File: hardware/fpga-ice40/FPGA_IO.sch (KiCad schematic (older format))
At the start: 1 part, among them U1 iCE40HX4K-TQ144

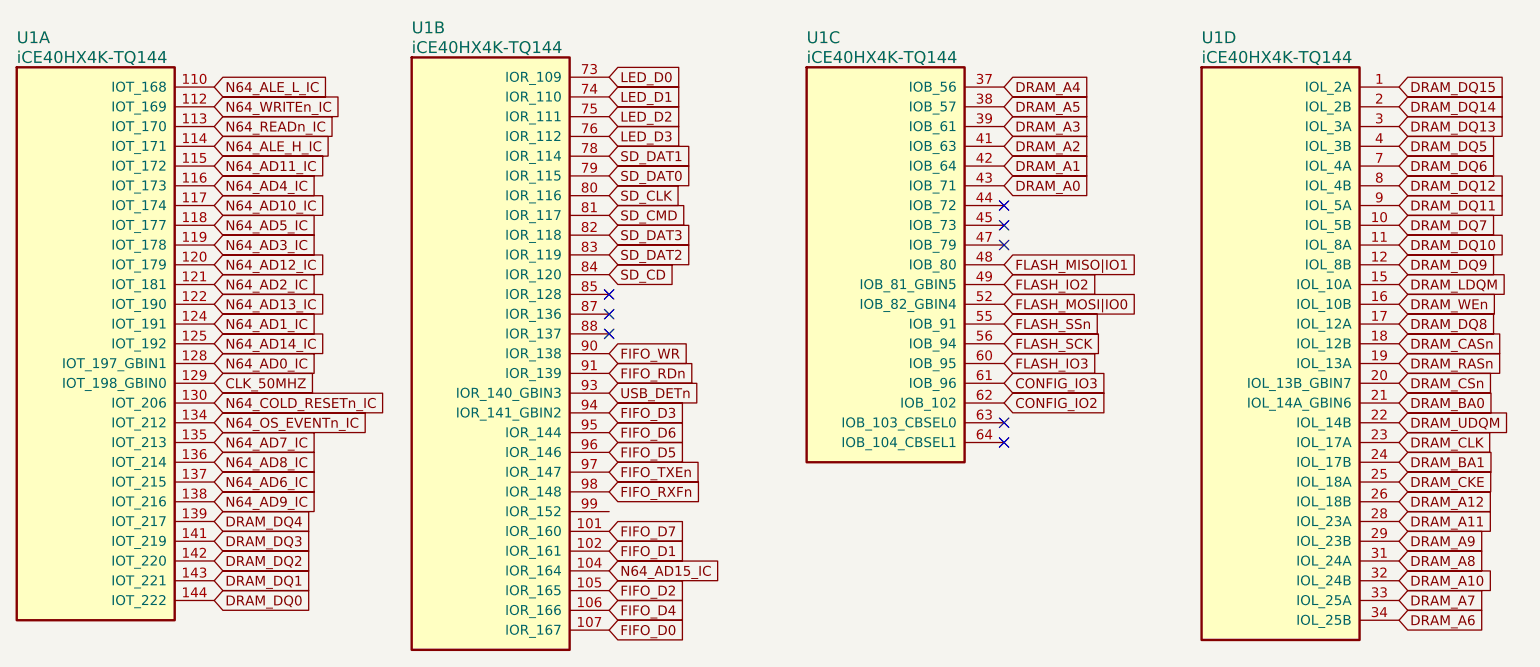
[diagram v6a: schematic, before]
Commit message: Routed N64, DRAM, FIFO, and SD card interfaces
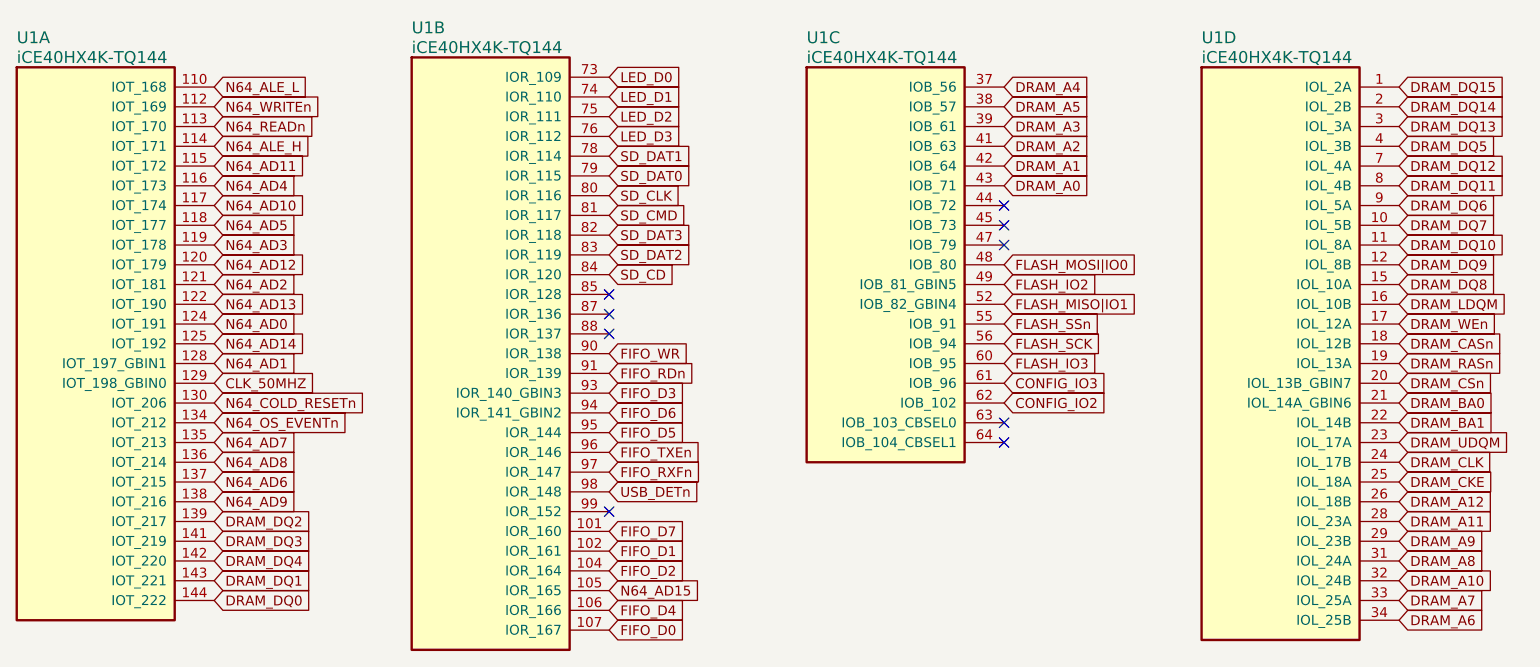
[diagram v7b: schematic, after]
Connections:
- net N64_AD15_IC is gone; now on net FIFO_D2: U1.104 (IOR_164)
- net DRAM_BA1: now also U1.22 (IOL_14B); no longer U1.24 (IOL_17B)
- net DRAM_CLK: now also U1.24 (IOL_17B); no longer U1.23 (IOL_17A)
- net DRAM_DQ11: now also U1.8 (IOL_4B); no longer U1.9 (IOL_5A)
- net DRAM_DQ12: now also U1.7 (IOL_4A); no longer U1.8 (IOL_4B)
- net DRAM_DQ2: now also U1.139 (IOT_217); no longer U1.142 (IOT_220)
- net DRAM_DQ4: now also U1.142 (IOT_220); no longer U1.139 (IOT_217)
- net DRAM_DQ6: now also U1.9 (IOL_5A); no longer U1.7 (IOL_4A)
- net DRAM_DQ8: now also U1.15 (IOL_10A); no longer U1.17 (IOL_12A)
- net DRAM_LDQM: now also U1.16 (IOL_10B); no longer U1.15 (IOL_10A)
- net DRAM_UDQM: now also U1.23 (IOL_17A); no longer U1.22 (IOL_14B)
- net DRAM_WEn: now also U1.17 (IOL_12A); no longer U1.16 (IOL_10B)
- net FIFO_D2: no longer U1.105 (IOR_165)
- net FIFO_D3: now also U1.93 (IOR_140_GBIN3); no longer U1.94 (IOR_141_GBIN2)
- net FIFO_D5: now also U1.95 (IOR_144); no longer U1.96 (IOR_146)
- net FIFO_D6: now also U1.94 (IOR_141_GBIN2); no longer U1.95 (IOR_144)
- net FIFO_RXFn: now also U1.97 (IOR_147); no longer U1.98 (IOR_148)
- net FIFO_TXEn: now also U1.96 (IOR_146); no longer U1.97 (IOR_147)
- net FLASH_MISO|IO1: now also U1.52 (IOB_82_GBIN4); no longer U1.48 (IOB_80)
- net FLASH_MOSI|IO0: now also U1.48 (IOB_80); no longer U1.52 (IOB_82_GBIN4)
- net USB_DETn: now also U1.98 (IOR_148); no longer U1.93 (IOR_140_GBIN3)
- net N64_AD0_IC renamed N64_AD1
- net N64_AD10_IC renamed N64_AD10
- net N64_AD11_IC renamed N64_AD11
- net N64_AD12_IC renamed N64_AD12
- net N64_AD13_IC renamed N64_AD13
- net N64_AD14_IC renamed N64_AD14
- net N64_AD1_IC renamed N64_AD0
- net N64_AD2_IC renamed N64_AD2
- net N64_AD3_IC renamed N64_AD3
- net N64_AD4_IC renamed N64_AD4
- net N64_AD5_IC renamed N64_AD5
- net N64_AD6_IC renamed N64_AD6
- net N64_AD7_IC renamed N64_AD7
- net N64_AD8_IC renamed N64_AD8
- net N64_AD9_IC renamed N64_AD9
- net N64_ALE_H_IC renamed N64_ALE_H
- net N64_ALE_L_IC renamed N64_ALE_L
- net N64_COLD_RESETn_IC renamed N64_COLD_RESETn
- net N64_OS_EVENTn_IC renamed N64_OS_EVENTn
- net N64_READn_IC renamed N64_READn
- net N64_WRITEn_IC renamed N64_WRITEn
- new net N64_AD15: U1.105 (IOR_165)
- no-connect marks 8 -> 9
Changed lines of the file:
@@
 Text GLabel 8850 5250 2    50   Input ~ 0
 DRAM_A8
-Text GLabel 4850 4400 2    50   Input ~ 0
+Text GLabel 4850 4900 2    50   Input ~ 0
 USB_DETn
-Text GLabel 4850 4800 2    50   Input ~ 0
+Text GLabel 4850 4700 2    50   Input ~ 0
 FIFO_TXEn
 Text GLabel 4850 4200 2    50   Input ~ 0
@@
 Text GLabel 4850 4300 2    50   Input ~ 0
 FIFO_RDn
-Text GLabel 4850 4900 2    50   Input ~ 0
+Text GLabel 4850 4800 2    50   Input ~ 0
 FIFO_RXFn
-Text GLabel 4850 4700 2    50   Input ~ 0
+Text GLabel 4850 4600 2    50   Input ~ 0
 FIFO_D5
 Text GLabel 4850 5100 2    50   Input ~ 0
 FIFO_D7
-Text GLabel 4850 4600 2    50   Input ~ 0
+Text GLabel 4850 4500 2    50   Input ~ 0
 FIFO_D6
 Text GLabel 4850 5500 2    50   Input ~ 0
 FIFO_D4
-Text GLabel 4850 4500 2    50   Input ~ 0
+Text GLabel 4850 4400 2    50   Input ~ 0
 FIFO_D3
-Text GLabel 4850 5400 2    50   Input ~ 0
+Text GLabel 4850 5300 2    50   Input ~ 0
 FIFO_D2
 Text GLabel 4850 5200 2    50   Input ~ 0
@@
 Text GLabel 6850 2950 2    50   Input ~ 0
 DRAM_A5
-Text GLabel 8850 4750 2    50   Input ~ 0
+Text GLabel 8850 4550 2    50   Input ~ 0
 DRAM_BA1
 Text GLabel 8850 4450 2    50   Input ~ 0
@@
 Text GLabel 8850 4150 2    50   Input ~ 0
 DRAM_CASn
+Text GLabel 8850 4050 2    50   Input ~ 0
+DRAM_WEn
 Text GLabel 8850 3950 2    50   Input ~ 0
-DRAM_WEn
-Text GLabel 8850 3850 2    50   Input ~ 0
 DRAM_LDQM
 Text GLabel 6850 3050 2    50   Input ~ 0
@@
 Text GLabel 8850 3550 2    50   Input ~ 0
 DRAM_DQ7
-Text GLabel 8850 3250 2    50   Input ~ 0
+Text GLabel 8850 3450 2    50   Input ~ 0
 DRAM_DQ6
 Text GLabel 8850 3150 2    50   Input ~ 0
 DRAM_DQ5
-Text GLabel 2850 5050 2    50   Input ~ 0
+Text GLabel 2850 5250 2    50   Input ~ 0
 DRAM_DQ4
 Text GLabel 2850 5150 2    50   Input ~ 0
 DRAM_DQ3
-Text GLabel 2850 5250 2    50   Input ~ 0
+Text GLabel 2850 5050 2    50   Input ~ 0
 DRAM_DQ2
 Text GLabel 2850 5350 2    50   Input ~ 0
@@
 Text GLabel 8850 4850 2    50   Input ~ 0
 DRAM_CKE
+Text GLabel 8850 4750 2    50   Input ~ 0
+DRAM_CLK
 Text GLabel 8850 4650 2    50   Input ~ 0
-DRAM_CLK
-Text GLabel 8850 4550 2    50   Input ~ 0
 DRAM_UDQM
 Text GLabel 8850 2850 2    50   Input ~ 0
@@
 Text GLabel 8850 3050 2    50   Input ~ 0
 DRAM_DQ13
+Text GLabel 8850 3250 2    50   Input ~ 0
+DRAM_DQ12
 Text GLabel 8850 3350 2    50   Input ~ 0
-DRAM_DQ12
-Text GLabel 8850 3450 2    50   Input ~ 0
 DRAM_DQ11
 Text GLabel 8850 3650 2    50   Input ~ 0
@@
 Text GLabel 8850 3750 2    50   Input ~ 0
 DRAM_DQ9
-Text GLabel 8850 4050 2    50   Input ~ 0
+Text GLabel 8850 3850 2    50   Input ~ 0
 DRAM_DQ8
 Text GLabel 2850 4650 2    50   Input ~ 0
-N64_AD7_IC
+N64_AD7
 Text GLabel 2850 4850 2    50   Input ~ 0
-N64_AD6_IC
+N64_AD6
 Text GLabel 2850 3550 2    50   Input ~ 0
-N64_AD5_IC
+N64_AD5
 Text GLabel 2850 3350 2    50   Input ~ 0
-N64_AD4_IC
+N64_AD4
 Text GLabel 2850 4550 2    50   Input ~ 0
-N64_OS_EVENTn_IC
+N64_OS_EVENTn
 Text GLabel 2850 4450 2    50   Input ~ 0
-N64_COLD_RESETn_IC
+N64_COLD_RESETn
 Text GLabel 2850 4750 2    50   Input ~ 0
-N64_AD8_IC
+N64_AD8
 Text GLabel 2850 4950 2    50   Input ~ 0
-N64_AD9_IC
+N64_AD9
 Text GLabel 2850 3450 2    50   Input ~ 0
-N64_AD10_IC
+N64_AD10
 Text GLabel 2850 3250 2    50   Input ~ 0
-N64_AD11_IC
+N64_AD11
 Text GLabel 2850 3750 2    50   Input ~ 0
-N64_AD12_IC
+N64_AD12
 Text GLabel 2850 3950 2    50   Input ~ 0
-N64_AD13_IC
+N64_AD13
 Text GLabel 2850 3050 2    50   Input ~ 0
-N64_READn_IC
+N64_READn
 Text GLabel 2850 2950 2    50   Input ~ 0
-N64_WRITEn_IC
+N64_WRITEn
 Text GLabel 2850 3150 2    50   Input ~ 0
-N64_ALE_H_IC
+N64_ALE_H
 Text GLabel 2850 2850 2    50   Input ~ 0
-N64_ALE_L_IC
+N64_ALE_L
 Text GLabel 2850 3650 2    50   Input ~ 0
-N64_AD3_IC
+N64_AD3
 Text GLabel 2850 3850 2    50   Input ~ 0
-N64_AD2_IC
-Text GLabel 4850 5300 2    50   Input ~ 0
-N64_AD15_IC
-Text GLabel 2850 4250 2    50   Input ~ 0
-N64_AD0_IC
+N64_AD2
+Text GLabel 4850 5400 2    50   Input ~ 0
+N64_AD15
+Text GLabel 2850 4050 2    50   Input ~ 0
+N64_AD0
 Text GLabel 6850 4250 2    50   Input ~ 0
 FLASH_IO3
 Text GLabel 6850 3850 2    50   Input ~ 0
 FLASH_IO2
+Text GLabel 6850 3950 2    50   Input ~ 0
+FLASH_MISO|IO1
 Text GLabel 6850 3750 2    50   Input ~ 0
-FLASH_MISO|IO1
-Text GLabel 6850 3950 2    50   Input ~ 0
 FLASH_MOSI|IO0
 Text GLabel 6850 4150 2    50   Input ~ 0
@@
 $EndComp
 Text GLabel 2850 4150 2    50   Input ~ 0
-N64_AD14_IC
-Text GLabel 2850 4050 2    50   Input ~ 0
-N64_AD1_IC
+N64_AD14
+Text GLabel 2850 4250 2    50   Input ~ 0
+N64_AD1
+NoConn ~ 4850 5000
 $EndSCHEMATC

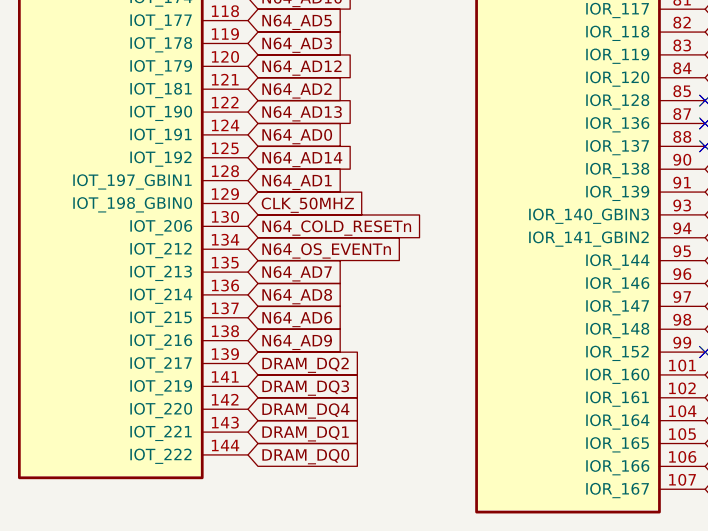
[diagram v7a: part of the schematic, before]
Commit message: Finished routing all nets, including power distribution
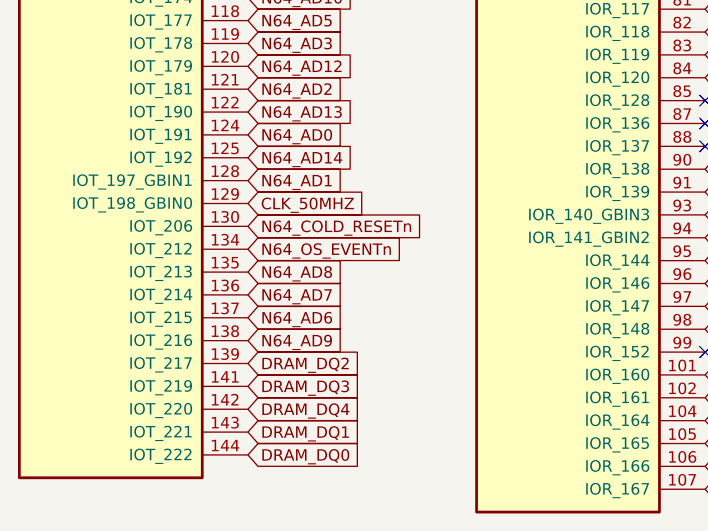
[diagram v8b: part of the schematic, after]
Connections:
- net N64_AD7: now also U1.136 (IOT_214); no longer U1.135 (IOT_213)
- net N64_AD8: now also U1.135 (IOT_213); no longer U1.136 (IOT_214)
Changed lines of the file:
@@
 Text GLabel 8850 3850 2    50   Input ~ 0
 DRAM_DQ8
-Text GLabel 2850 4650 2    50   Input ~ 0
+Text GLabel 2850 4750 2    50   Input ~ 0
 N64_AD7
 Text GLabel 2850 4850 2    50   Input ~ 0
@@
 Text GLabel 2850 4450 2    50   Input ~ 0
 N64_COLD_RESETn
-Text GLabel 2850 4750 2    50   Input ~ 0
+Text GLabel 2850 4650 2    50   Input ~ 0
 N64_AD8
 Text GLabel 2850 4950 2    50   Input ~ 0
